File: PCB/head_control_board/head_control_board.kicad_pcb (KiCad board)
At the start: 2 copper layers, 104.5 x 72.5 mm, 64 parts, among them Q1 AO3401A, U1 TPS63070RNMR, U2 TPS63070RNMR, U3 SN74AHCT245PWR, U4 ESP32-S3-WROOM-1(N16R8)

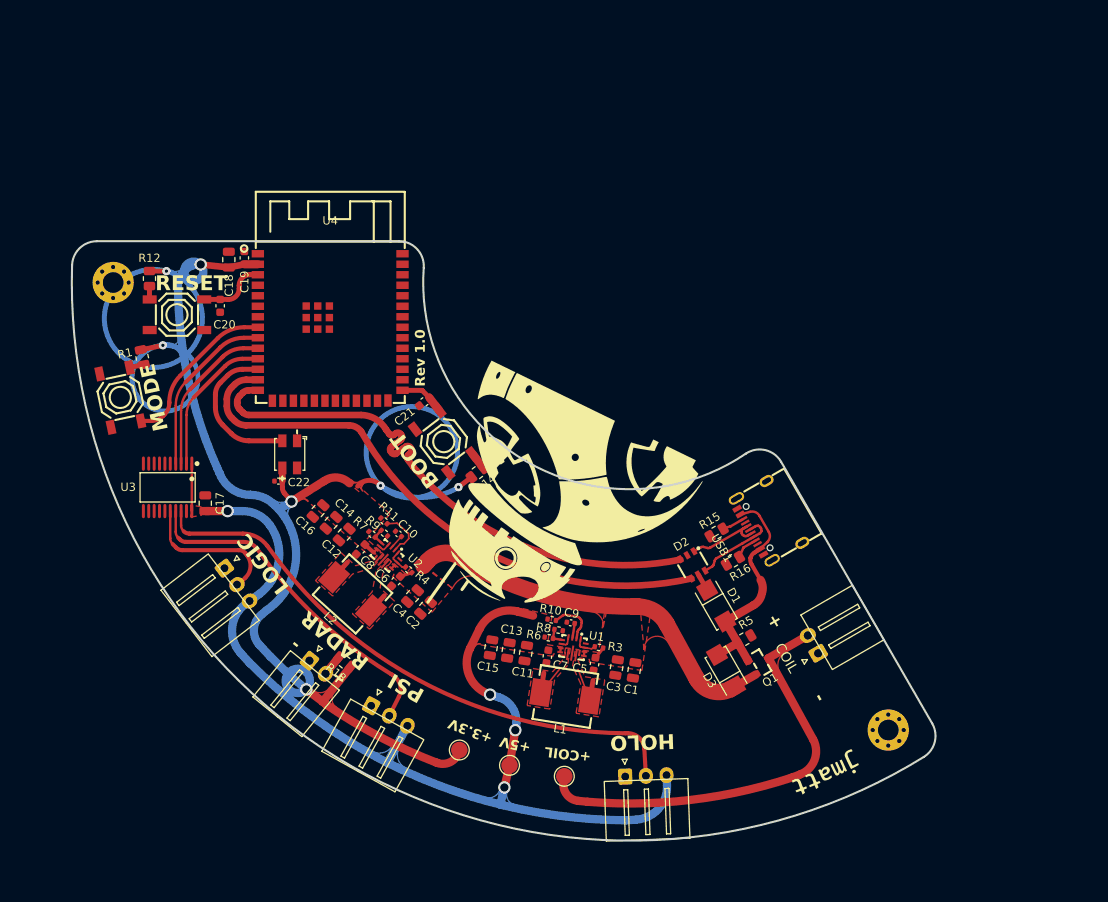
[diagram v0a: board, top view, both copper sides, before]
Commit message: Finish GND planes
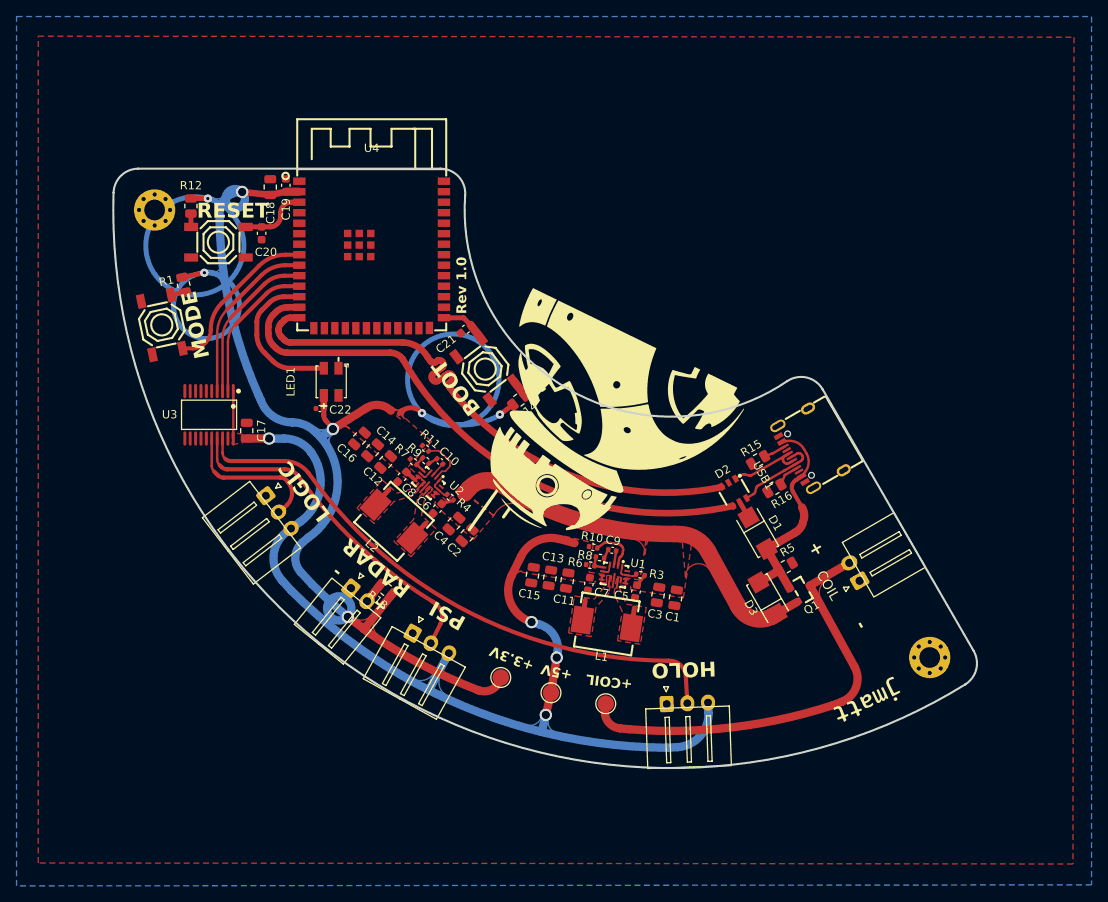
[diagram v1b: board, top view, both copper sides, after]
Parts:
- COIL1, RADAR1: footprint Connector_JST:JST_XH_S2B-XH-A-1_1x02_P2.50mm_Horizontal -> jmatt:JST_XH_S2B-XH-A-1_1x02_P2.50mm_Horizontal
- HOLO1, LOGIC1, PSI1: footprint Connector_JST:JST_XH_S3B-XH-A-1_1x03_P2.50mm_Horizontal -> jmatt:JST_XH_S3B-XH-A-1_1x03_P2.50mm_Horizontal
- moved D1 10.1 mm to (137.2, 85.0)
- moved BOOT1 10.1 mm to (104.2, 65.1)
- moved C11 10.1 mm to (114.2, 90.7)
- moved C13 10.1 mm to (112.1, 90.4)
- moved C7 10.1 mm to (116.8, 91.1)
- moved HOLO1 10.1 mm to (126.2, 105.6)
- moved R6 10.1 mm to (116.9, 88.8)
- moved R7 10.1 mm to (95.6, 76.3)
- moved RESET1 10.1 mm to (72.0, 49.8)
- moved U2 10.1 mm to (97.5, 78.8)
- moved U3 10.1 mm to (70.8, 70.6)
- moved SELECT1 10.1 mm to (65.1, 59.8)
- moved C18 10.1 mm to (78.2, 43.1)
- moved C21 10.1 mm to (101.9, 60.3)
- moved C12 10.1 mm to (92.2, 76.4)
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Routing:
- net Net-(U1-L1): track 6.43 -> 2.44 mm
- net Net-(U1-L2): track 6.06 -> 2.40 mm
- net GND: track 3.13 -> 5.41 mm
- net Net-(Q1-G): track 27.7 -> 27.1 mm
- added copper zone on B.Cu, net GND
- added copper zone on F.Cu, net GND
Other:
- board text added: "{ "ViaStitching": "0.2", "stitch_zone_0": { "HSpacing": "2.5", "VSpacing": "2.5", "Clearance": "1", "Randomize": false }, "stitch_zone_1": { "HSpacing": "2.5", "VSpacing": "2.5", "Clearance": ".2", "Randomize": false } }"

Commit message: Add via stitching
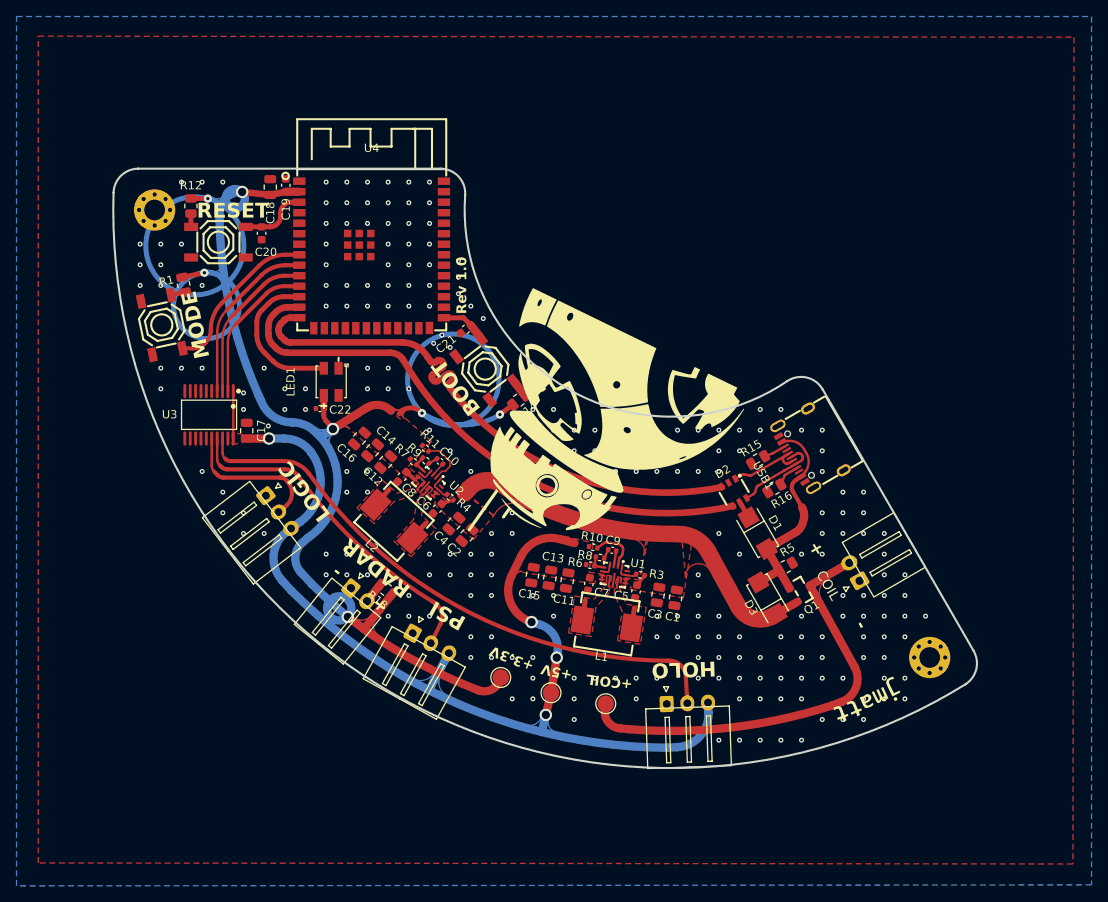
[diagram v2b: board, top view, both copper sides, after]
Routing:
- net GND: vias 0 -> 242

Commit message: Start passive component selection
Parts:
- C17: value 10uF -> 0.1uF
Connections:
- U3 pad 5: unconnected-(U3-A4-Pad5) -> GND
- U3 pad 6: unconnected-(U3-A5-Pad6) -> GND
- U3 pad 7: unconnected-(U3-A6-Pad7) -> GND
- U3 pad 8: unconnected-(U3-A7-Pad8) -> GND
- U3 pad 9: unconnected-(U3-A8-Pad9) -> GND
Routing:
- net GND: track 5.41 -> 11.0 mm, vias 242 -> 254
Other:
- board text removed: "{ "ViaStitching": "0.2", "stitch_zone_0": { "HSpacing": "2.5", "VSpacing": "2.5", "Clearance": "1", "Randomize": false }, "stitch_zone_1": { "HSpacing": "2.5", "VSpacing": "2.5", "Clearance": ".2", "Randomize": false } }"

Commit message: Finish component selection
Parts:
- R13: value 60 -> 68
- R6, R7, R8, R9: footprint Resistor_SMD:R_0402_1005Metric -> Resistor_SMD:R_0603_1608Metric
- moved R11 0.90 mm to (97.3, 73.8)
- moved R10 0.88 mm to (117.2, 85.8)
- moved C9 0.83 mm to (120.4, 87.1), turned to 81 degrees
- moved C10 0.78 mm to (99.4, 76.7), turned to 48 degrees
- moved R8 0.61 mm to (118.3, 87.3)
- moved R9 0.59 mm to (97.5, 75.8)
- moved R6 0.51 mm to (116.4, 88.8)
- moved R7 0.49 mm to (95.2, 76.0)
- moved C16 0.26 mm to (88.8, 73.7)
- moved C12 0.24 mm to (92.0, 76.5)
- moved C14 0.23 mm to (90.5, 75.1)
- moved C11 0.20 mm to (114.1, 90.9)
- moved C13 0.18 mm to (112.0, 90.5)
- moved C15 0.16 mm to (109.9, 90.2)
- moved C7 0.09 mm to (116.8, 91.2)
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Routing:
- net GND: track 11.0 -> 15.3 mm, vias 254 -> 255
- net +5V: track 129.6 -> 133.2 mm
- net +3.3V: track 167.0 -> 168.5 mm
- net Net-(U2-PG): track 5.95 -> 6.86 mm
- net Net-(U1-PG): track 5.85 -> 6.75 mm
- net Net-(U2-FB): track 2.21 -> 2.99 mm
- net Net-(U1-FB): track 2.24 -> 3.02 mm
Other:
- board text added: "JLCJLCJLCJLC"

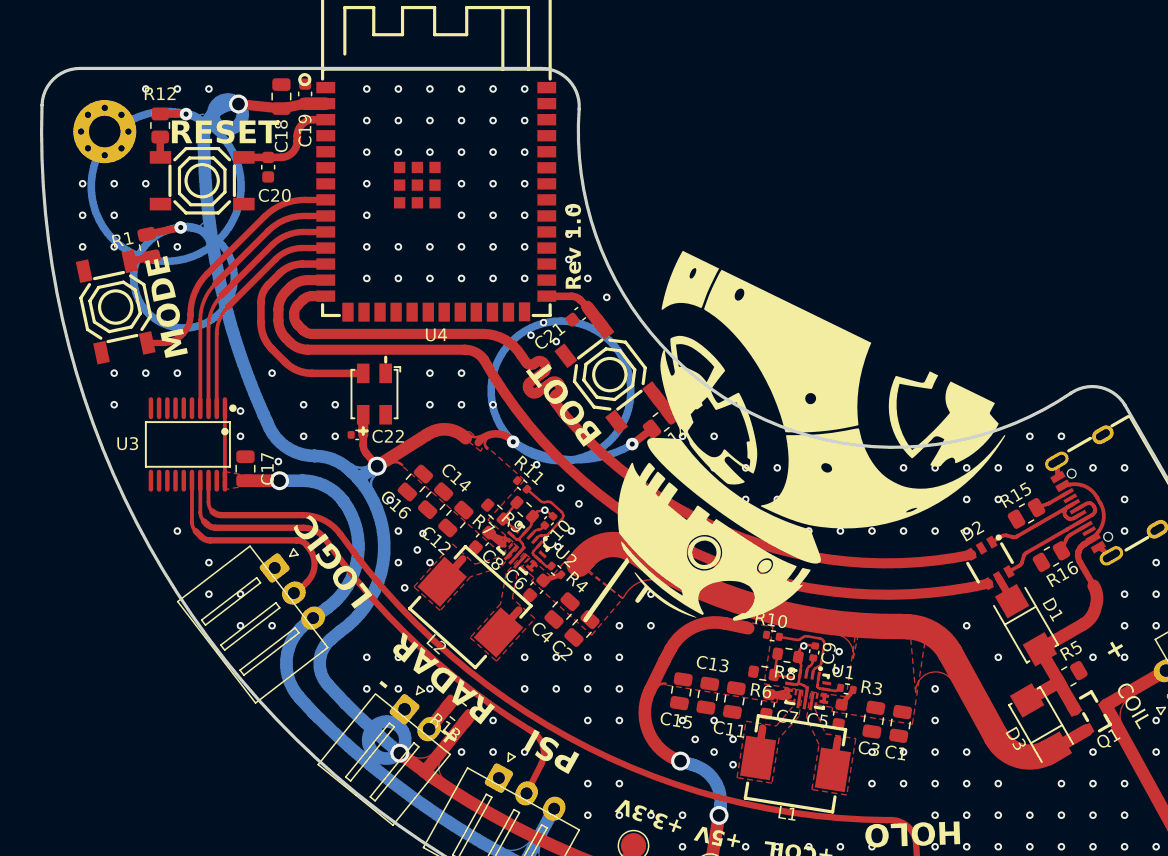
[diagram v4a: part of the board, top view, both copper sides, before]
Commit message: Component cost optimization
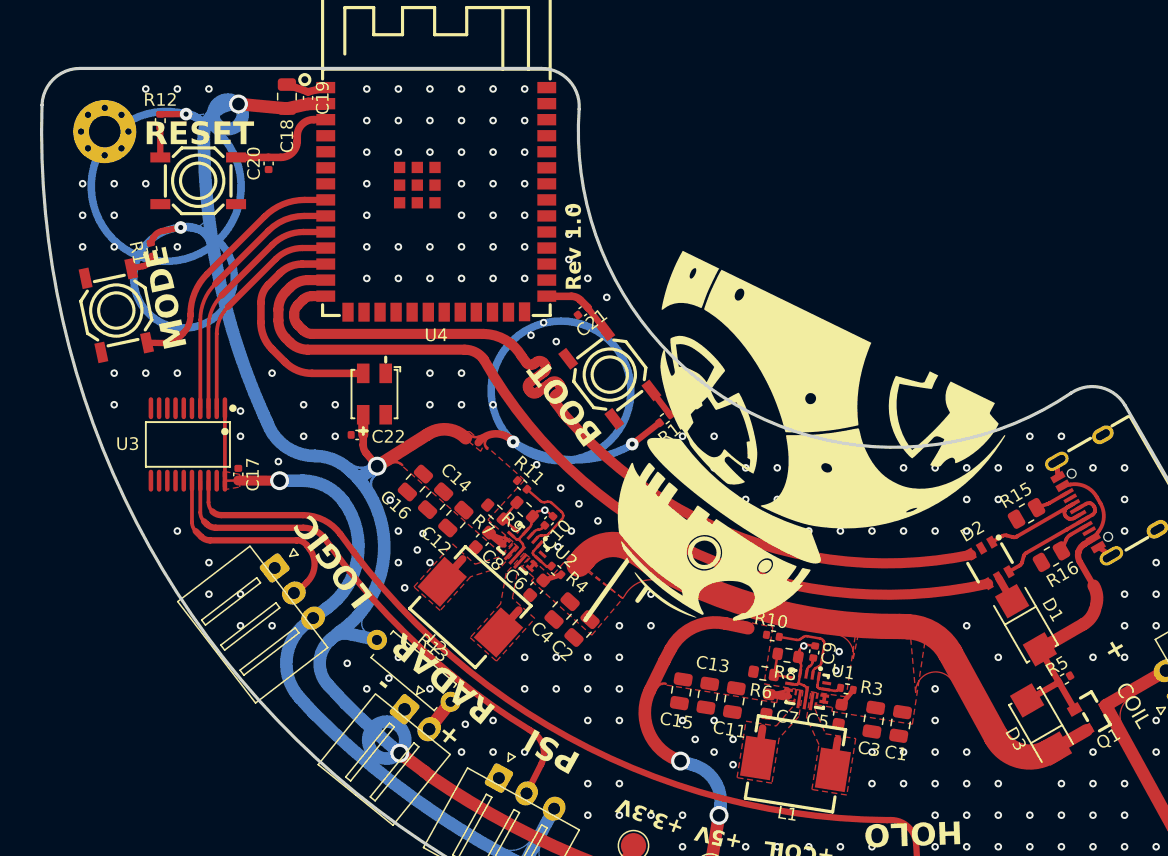
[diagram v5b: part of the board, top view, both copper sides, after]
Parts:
- BOOT1, RESET1, SELECT1: footprint LCSC:SW-SMD_4P-L5.1-W5.1-P3.70-LS6.5-TL-2 -> LCSC:SW-SMD_4P-L5.2-W5.2-P3.70-LS6.4
- C17: value 0.1uF -> 100nF; footprint Capacitor_SMD:C_0805_2012Metric -> Capacitor_SMD:C_0402_1005Metric
- C19, C20, C21: value 0.1uF -> 100nF; footprint Capacitor_SMD:C_0603_1608Metric -> Capacitor_SMD:C_0402_1005Metric
- R1, R12, R14, R5: footprint Resistor_SMD:R_0805_2012Metric -> Resistor_SMD:R_0402_1005Metric
- R13: footprint Resistor_SMD:R_0805_2012Metric -> Resistor_THT:R_Axial_DIN0207_L6.3mm_D2.5mm_P7.62mm_Horizontal
- moved R13 8.58 mm to (85.8, 86.1), turned to -40 degrees
- moved C17 0.73 mm to (74.8, 73.0)
- moved C18 0.44 mm to (78.7, 43.1)
- moved R5 0.40 mm to (140.2, 89.2)
- moved C19 0.39 mm to (80.3, 43.2)
- moved R14 0.39 mm to (108.6, 68.6)
- moved R12 0.38 mm to (68.7, 45.0)
- moved R1 0.37 mm to (68.0, 55.2)
- moved RESET1 0.32 mm to (71.7, 49.8)
- moved C20 0.29 mm to (77.2, 48.4)
- moved C21 0.28 mm to (102.1, 60.1)
- moved SELECT1 0.28 mm to (65.2, 60.0)
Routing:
- net GND: track 15.3 -> 18.5 mm, vias 255 -> 256
- net +5V: track 133.2 -> 134.9 mm
- net +3.3V: track 168.5 -> 167.0 mm
- net Net-(RESET1-A): track 1.62 -> 2.44 mm
- net Net-(RESET1-B): track 8.25 -> 8.90 mm
